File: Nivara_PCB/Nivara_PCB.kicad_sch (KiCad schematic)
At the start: 16 parts, among them J1 NPN_IN, J11 RELAY, J12 Analaog_In, J2 PNP_IN, J3 D_IN, J4 Analaog_In, J5 RUN/STOP, J6 FUENTE, J7 NPN_OUT, J8 PNP_OUT, J9 RS485, U4 2920L185DR

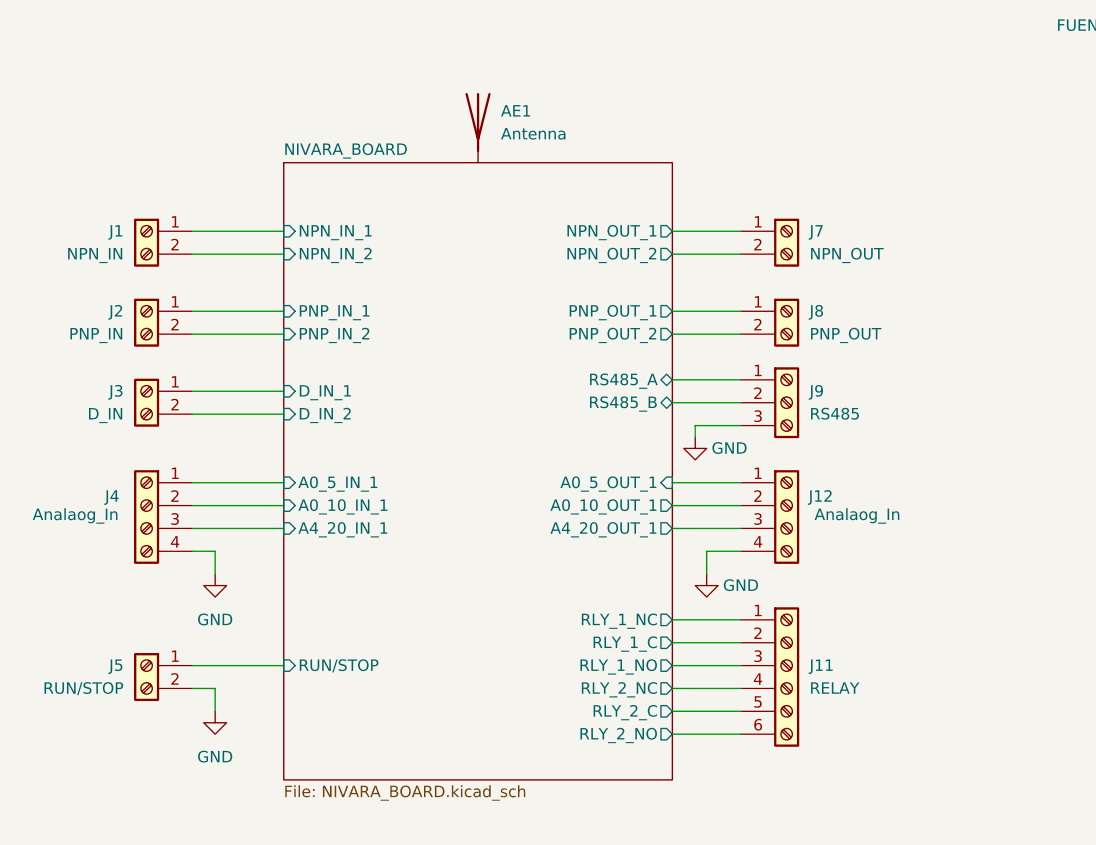
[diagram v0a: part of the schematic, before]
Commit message: Cambios en las mediciones análogas.
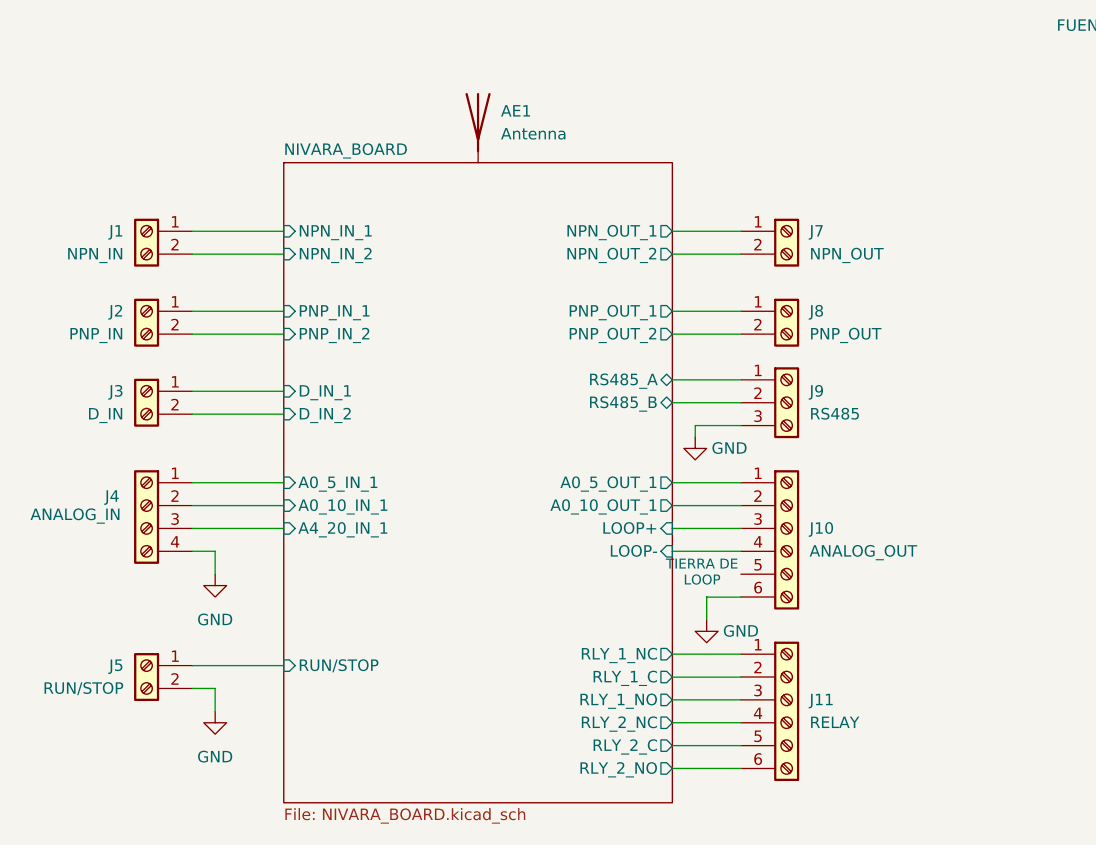
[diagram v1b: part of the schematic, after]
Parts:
- removed J12: Analaog_In, TerminalBlock:TerminalBlock_bornier-4_P5.08mm, symbol Connector:Screw_Terminal_01x04
- added J10: ANALOG_OUT, TerminalBlock:TerminalBlock_bornier-6_P5.08mm, symbol Connector:Screw_Terminal_01x06
- J4: value Analaog_In -> ANALOG_IN
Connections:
- net GND: now also J10.6 (Pin_6)
- net NIVARA_BOARD/A0_10_OUT_1: now also J10.2 (Pin_2)
- net NIVARA_BOARD/A0_5_OUT_1: now also J10.1 (Pin_1)
- new net NIVARA_BOARD/LOOP+: J10.3 (Pin_3)
- new net NIVARA_BOARD/LOOP-: J10.4 (Pin_4)
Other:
- sheet NIVARA_BOARD ports: added LOOP+, LOOP-; removed A4_20_OUT_1
- note added: "TIERRA DE LOOP"
- moved on the sheet: J11
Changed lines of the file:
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@@
+		)
+	)
+	(text "TIERRA DE\nLOOP"
+		(exclude_from_sim no)
+		(at 87.122 106.68 0)
+		(effects
+			(font
+				(size 1.1 1.1)
+			)
 		)
 	)
@@
 	(wire
 		(pts
+			(xy 87.63 109.22) (xy 91.44 109.22)
+		)
+		(stroke
+			(width 0)
+			(type default)
+		)
+	)
+	(wire
+		(pts
 			(xy 83.82 87.63) (xy 91.44 87.63)
 		)
@@
 	(wire
 		(pts
-			(xy 83.82 119.38) (xy 91.44 119.38)
+			(xy 83.82 123.19) (xy 91.44 123.19)
 		)
 		(stroke
@@
 	(wire
 		(pts
-			(xy 83.82 121.92) (xy 91.44 121.92)
+			(xy 83.82 125.73) (xy 91.44 125.73)
 		)
 		(stroke
@@
 	(wire
 		(pts
-			(xy 83.82 114.3) (xy 91.44 114.3)
+			(xy 83.82 118.11) (xy 91.44 118.11)
 		)
 		(stroke
@@
 	(wire
 		(pts
+			(xy 83.82 104.14) (xy 91.44 104.14)
+		)
+		(stroke
+			(width 0)
+			(type default)
+		)
+	)
+	(wire
+		(pts
 			(xy 83.82 101.6) (xy 91.44 101.6)
 		)
@@
 	(wire
 		(pts
-			(xy 83.82 116.84) (xy 91.44 116.84)
+			(xy 83.82 120.65) (xy 91.44 120.65)
 		)
 		(stroke
@@
 	(wire
 		(pts
-			(xy 83.82 111.76) (xy 91.44 111.76)
+			(xy 83.82 115.57) (xy 91.44 115.57)
 		)
 		(stroke
@@
 	(wire
 		(pts
-			(xy 87.63 104.14) (xy 91.44 104.14)
-		)
-		(stroke
-			(width 0)
-			(type default)
-		)
-	)
-	(wire
-		(pts
-			(xy 87.63 106.68) (xy 87.63 104.14)
-		)
-		(stroke
-			(width 0)
-			(type default)
-		)
-	)
-	(wire
-		(pts
-			(xy 83.82 124.46) (xy 91.44 124.46)
+			(xy 87.63 111.76) (xy 87.63 109.22)
+		)
+		(stroke
+			(width 0)
+			(type default)
+		)
+	)
+	(wire
+		(pts
+			(xy 83.82 128.27) (xy 91.44 128.27)
 		)
 		(stroke
@@
 	)
 	(symbol
+		(lib_id "Connector:Screw_Terminal_01x06")
+		(at 96.52 101.6 0)
+		(unit 1)
+		(exclude_from_sim no)
+		(in_bom yes)
+		(on_board yes)
+		(dnp no)
+		(property "Reference" "J10"
+			(at 99.06 101.5999 0)
+			(effects
+				(font
+					(size 1.27 1.27)
+				)
+				(justify left)
+			)
+		)
+		(property "Value" "ANALOG_OUT"
+			(at 99.06 104.1399 0)
+			(effects
+				(font
+					(size 1.27 1.27)
+				)
+				(justify left)
+			)
+		)
+		(property "Footprint" "TerminalBlock:TerminalBlock_bornier-6_P5.08mm"
+			(at 96.52 101.6 0)
+			(effects
+				(font
+					(size 1.27 1.27)
+				)
+				(hide yes)
+			)
+		)
+		(property "Datasheet" "~"
+			(at 96.52 101.6 0)
+			(effects
+				(font
+					(size 1.27 1.27)
+				)
+				(hide yes)
+			)
+		)
+		(property "Description" "Generic screw terminal, single row, 01x06, script generated (kicad-library-utils/schlib/autogen/connector/)"
+			(at 96.52 101.6 0)
+			(effects
+				(font
+					(size 1.27 1.27)
+				)
+				(hide yes)
+			)
+		)
+		(pin "4"
+		)
+		(pin "1"
+		)
+		(pin "6"
+		)
+		(pin "3"
+		)
+		(pin "5"
+		)
+		(pin "2"
+		)
+		(instances
+			(project "Nivara_PCB"
+				(path "/13184db0-a71d-4054-b13a-bbf46d2b100d"
+					(reference "J10")
+					(unit 1)
+				)
+			)
+		)
+	)
+	(symbol
 		(lib_id "power:GND")
 		(at 173.99 102.87 0)
@@
 	(symbol
 		(lib_id "power:GND")
-		(at 87.63 106.68 0)
+		(at 87.63 111.76 0)
 		(unit 1)
 		(exclude_from_sim no)
@@
 		(dnp no)
 		(property "Reference" "#PWR06"
-			(at 87.63 113.03 0)
+			(at 87.63 118.11 0)
 			(effects
 				(font
@@
 		)
 		(property "Value" "GND"
-			(at 91.44 107.95 0)
+			(at 91.44 113.03 0)
 			(effects
 				(font
@@
 		)
 		(property "Footprint" ""
-			(at 87.63 106.68 0)
+			(at 87.63 111.76 0)
 			(effects
 				(font
@@
 		)
 		(property "Datasheet" ""
-			(at 87.63 106.68 0)
+			(at 87.63 111.76 0)
 			(effects
 				(font
@@
 		)
 		(property "Description" "Power symbol creates a global label with name \"GND\" , ground"
-			(at 87.63 106.68 0)
+			(at 87.63 111.76 0)
 			(effects
 				(font
@@
 	(symbol
 		(lib_id "Connector:Screw_Terminal_01x06")
-		(at 96.52 116.84 0)
+		(at 96.52 120.65 0)
 		(unit 1)
 		(exclude_from_sim no)
@@
 		(dnp no)
 		(property "Reference" "J11"
-			(at 99.06 116.8399 0)
+			(at 99.06 120.6499 0)
 			(effects
 				(font
@@
 		)
 		(property "Value" "RELAY"
-			(at 99.06 119.3799 0)
+			(at 99.06 123.1899 0)
 			(effects
 				(font
@@
 		)
 		(property "Footprint" "TerminalBlock:TerminalBlock_bornier-6_P5.08mm"
-			(at 96.52 116.84 0)
+			(at 96.52 120.65 0)
 			(effects
 				(font
@@
 		)
 		(property "Datasheet" "~"
-			(at 96.52 116.84 0)
+			(at 96.52 120.65 0)
 			(effects
 				(font
@@
 		)
 		(property "Description" "Generic screw terminal, single row, 01x06, script generated (kicad-library-utils/schlib/autogen/connector/)"
-			(at 96.52 116.84 0)
+			(at 96.52 120.65 0)
 			(effects
 				(font
@@
 			)
 		)
-		(property "Value" "Analaog_In"
+		(property "Value" "ANALOG_IN"
 			(at 17.526 100.076 0)
 			(effects
@@
 				(path "/13184db0-a71d-4054-b13a-bbf46d2b100d"
 					(reference "J8")
-					(unit 1)
-				)
-			)
-		)
-	)
-	(symbol
-		(lib_id "Connector:Screw_Terminal_01x04")
-		(at 96.52 99.06 0)
-		(unit 1)
-		(exclude_from_sim no)
-		(in_bom yes)
-		(on_board yes)
-		(dnp no)
-		(property "Reference" "J12"
-			(at 100.33 98.044 0)
-			(effects
-				(font
-					(size 1.27 1.27)
-				)
-			)
-		)
-		(property "Value" "Analaog_In"
-			(at 104.394 100.076 0)
-			(effects
-				(font
-					(size 1.27 1.27)
-				)
-			)
-		)
-		(property "Footprint" "TerminalBlock:TerminalBlock_bornier-4_P5.08mm"
-			(at 96.52 99.06 0)
-			(effects
-				(font
-					(size 1.27 1.27)
-				)
-				(hide yes)
-			)
-		)
-		(property "Datasheet" "~"
-			(at 96.52 99.06 0)
-			(effects
-				(font
-					(size 1.27 1.27)
-				)
-				(hide yes)
-			)
-		)
-		(property "Description" "Generic screw terminal, single row, 01x04, script generated (kicad-library-utils/schlib/autogen/connector/)"
-			(at 96.52 99.06 0)
-			(effects
-				(font
-					(size 1.27 1.27)
-				)
-				(hide yes)
-			)
-		)
-		(pin "3"
-		)
-		(pin "2"
-		)
-		(pin "1"
-		)
-		(pin "4"
-		)
-		(instances
-			(project "Nivara_PCB"
-				(path "/13184db0-a71d-4054-b13a-bbf46d2b100d"
-					(reference "J12")
 					(unit 1)
 				)
@@
 	(sheet
 		(at 40.64 60.96)
-		(size 43.18 68.58)
+		(size 43.18 71.12)
 		(exclude_from_sim no)
 		(in_bom yes)
@@
 		)
 		(property "Sheetfile" "NIVARA_BOARD.kicad_sch"
-			(at 40.64 130.1246 0)
+			(at 40.64 132.6646 0)
 			(effects
 				(font
@@
 			)
 		)
-		(pin "A4_20_OUT_1" output
-			(at 83.82 101.6 0)
-			(effects
-				(font
-					(size 1.27 1.27)
-				)
-				(justify right)
-			)
-		)
 		(pin "D_IN_1" input
 			(at 40.64 86.36 180)
@@
 		)
 		(pin "RLY_1_C" output
-			(at 83.82 114.3 0)
+			(at 83.82 118.11 0)
 			(effects
 				(font
@@
 		)
 		(pin "RLY_1_NC" output
-			(at 83.82 111.76 0)
+			(at 83.82 115.57 0)
 			(effects
 				(font
@@
 		)
 		(pin "RLY_1_NO" output
-			(at 83.82 116.84 0)
+			(at 83.82 120.65 0)
 			(effects
 				(font
@@
 		)
 		(pin "RLY_2_C" output
-			(at 83.82 121.92 0)
+			(at 83.82 125.73 0)
 			(effects
 				(font
@@
 		)
 		(pin "RLY_2_NC" output
-			(at 83.82 119.38 0)
+			(at 83.82 123.19 0)
 			(effects
 				(font
@@
 		)
 		(pin "RLY_2_NO" output
-			(at 83.82 124.46 0)
+			(at 83.82 128.27 0)
 			(effects
 				(font
@@
 			)
 		)
-		(pin "A0_5_OUT_1" input
+		(pin "A0_5_OUT_1" output
 			(at 83.82 96.52 0)
 			(effects
 				(font
+					(size 1.27 1.27)
+				)
+				(justify right)
+			)
+		)
+		(pin "LOOP+" input
+			(at 83.82 101.6 0)
+			(effects
+				(font
+					(size 1.27 1.27)
+				)
+				(justify right)
+			)
+		)
+		(pin "LOOP-" input
+			(at 83.82 104.14 0)
+			(effects
+				(font

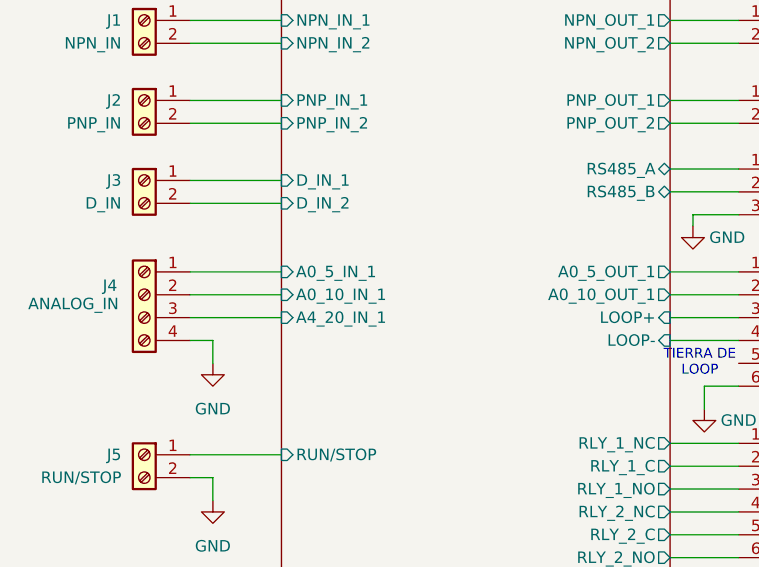
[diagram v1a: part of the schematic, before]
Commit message: Cambios en las salidas analogicas, ya que el ESP32 S3 no tiene DAC
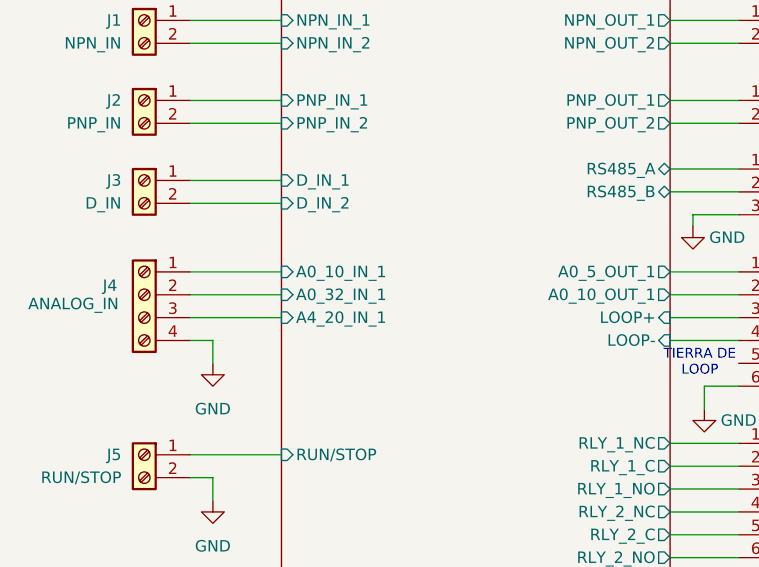
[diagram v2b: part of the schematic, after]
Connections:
- net NIVARA_BOARD/A0_5_IN_1 is gone; now on net NIVARA_BOARD/A0_10_IN_1: J4.1 (Pin_1)
- net NIVARA_BOARD/A0_10_IN_1: no longer J4.2 (Pin_2)
- new net NIVARA_BOARD/A0_32_IN_1: J4.2 (Pin_2)
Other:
- sheet NIVARA_BOARD ports: added A0_32_IN_1; removed A0_5_IN_1
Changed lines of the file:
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@@
+	(wire
+		(pts
+			(xy 33.02 121.92) (xy 33.02 119.38)
+		)
+		(stroke
+			(width 0)
+			(type default)
+		)
+	)
+	(wire
+		(pts
+			(xy 83.82 80.01) (xy 91.44 80.01)
+		)
+		(stroke
+			(width 0)
+			(type default)
+		)
+	)
+	(wire
+		(pts
+			(xy 160.02 43.18) (xy 160.02 52.07)
+		)
+		(stroke
+			(width 0)
+			(type default)
+		)
+	)
+	(wire
+		(pts
+			(xy 83.82 118.11) (xy 91.44 118.11)
+		)
+		(stroke
+			(width 0)
+			(type default)
+		)
+	)
+	(wire
+		(pts
+			(xy 83.82 96.52) (xy 91.44 96.52)
+		)
+		(stroke
+			(width 0)
+			(type default)
+		)
+	)
+	(wire
+		(pts
+			(xy 140.97 43.18) (xy 144.78 43.18)
+		)
+		(stroke
+			(width 0)
+			(type default)
+		)
+	)
+	(wire
+		(pts
+			(xy 83.82 104.14) (xy 91.44 104.14)
+		)
+		(stroke
+			(width 0)
+			(type default)
+		)
+	)
+	(wire
+		(pts
+			(xy 83.82 101.6) (xy 91.44 101.6)
+		)
+		(stroke
+			(width 0)
+			(type default)
+		)
+	)
+	(wire
+		(pts
+			(xy 160.02 35.56) (xy 160.02 43.18)
+		)
+		(stroke
+			(width 0)
+			(type default)
+		)
+	)
+	(wire
+		(pts
+			(xy 33.02 106.68) (xy 33.02 104.14)
+		)
+		(stroke
+			(width 0)
+			(type default)
+		)
+	)
+	(wire
+		(pts
+			(xy 83.82 99.06) (xy 91.44 99.06)
+		)
+		(stroke
+			(width 0)
+			(type default)
+		)
+	)
+	(wire
+		(pts
+			(xy 30.48 116.84) (xy 40.64 116.84)
+		)
+		(stroke
+			(width 0)
+			(type default)
+		)
+	)
+	(wire
+		(pts
+			(xy 30.48 96.52) (xy 40.64 96.52)
+		)
+		(stroke
+			(width 0)
+			(type default)
+		)
+	)
+	(wire
+		(pts
+			(xy 30.48 68.58) (xy 40.64 68.58)
+		)
+		(stroke
+			(width 0)
+			(type default)
+		)
+	)
+	(wire
+		(pts
+			(xy 86.36 91.44) (xy 86.36 90.17)
+		)
+		(stroke
+			(width 0)
+			(type default)
+		)
+	)
+	(wire
+		(pts
+			(xy 30.48 71.12) (xy 40.64 71.12)
+		)
+		(stroke
+			(width 0)
+			(type default)
+		)
+	)
+	(wire
+		(pts
+			(xy 162.56 90.17) (xy 162.56 93.98)
+		)
+		(stroke
+			(width 0)
+			(type default)
+		)
+	)
+	(wire
+		(pts
+			(xy 83.82 120.65) (xy 91.44 120.65)
+		)
+		(stroke
+			(width 0)
+			(type default)
+		)
+	)
+	(wire
+		(pts
+			(xy 83.82 71.12) (xy 91.44 71.12)
+		)
+		(stroke
+			(width 0)
+			(type default)
+		)
+	)
+	(wire
+		(pts
+			(xy 83.82 68.58) (xy 91.44 68.58)
+		)
+		(stroke
+			(width 0)
+			(type default)
+		)
+	)
+	(wire
+		(pts
+			(xy 83.82 85.09) (xy 91.44 85.09)
+		)
+		(stroke
+			(width 0)
+			(type default)
+		)
+	)
+	(wire
+		(pts
+			(xy 30.48 86.36) (xy 40.64 86.36)
+		)
+		(stroke
+			(width 0)
+			(type default)
+		)
+	)
+	(wire
+		(pts
+			(xy 30.48 80.01) (xy 40.64 80.01)
+		)
+		(stroke
+			(width 0)
+			(type default)
+		)
+	)
 	(wire
 		(pts
 			(xy 30.48 99.06) (xy 40.64 99.06)
-		)
-		(stroke
-			(width 0)
-			(type default)
-		)
-	)
-	(wire
-		(pts
-			(xy 33.02 121.92) (xy 33.02 119.38)
-		)
-		(stroke
-			(width 0)
-			(type default)
-		)
-	)
-	(wire
-		(pts
-			(xy 83.82 80.01) (xy 91.44 80.01)
-		)
-		(stroke
-			(width 0)
-			(type default)
-		)
-	)
-	(wire
-		(pts
-			(xy 160.02 43.18) (xy 160.02 52.07)
-		)
-		(stroke
-			(width 0)
-			(type default)
-		)
-	)
-	(wire
-		(pts
-			(xy 83.82 118.11) (xy 91.44 118.11)
-		)
-		(stroke
-			(width 0)
-			(type default)
-		)
-	)
-	(wire
-		(pts
-			(xy 83.82 96.52) (xy 91.44 96.52)
-		)
-		(stroke
-			(width 0)
-			(type default)
-		)
-	)
-	(wire
-		(pts
-			(xy 140.97 43.18) (xy 144.78 43.18)
-		)
-		(stroke
-			(width 0)
-			(type default)
-		)
-	)
-	(wire
-		(pts
-			(xy 83.82 104.14) (xy 91.44 104.14)
-		)
-		(stroke
-			(width 0)
-			(type default)
-		)
-	)
-	(wire
-		(pts
-			(xy 83.82 101.6) (xy 91.44 101.6)
-		)
-		(stroke
-			(width 0)
-			(type default)
-		)
-	)
-	(wire
-		(pts
-			(xy 160.02 35.56) (xy 160.02 43.18)
-		)
-		(stroke
-			(width 0)
-			(type default)
-		)
-	)
-	(wire
-		(pts
-			(xy 33.02 106.68) (xy 33.02 104.14)
-		)
-		(stroke
-			(width 0)
-			(type default)
-		)
-	)
-	(wire
-		(pts
-			(xy 30.48 96.52) (xy 40.64 96.52)
-		)
-		(stroke
-			(width 0)
-			(type default)
-		)
-	)
-	(wire
-		(pts
-			(xy 83.82 99.06) (xy 91.44 99.06)
-		)
-		(stroke
-			(width 0)
-			(type default)
-		)
-	)
-	(wire
-		(pts
-			(xy 30.48 116.84) (xy 40.64 116.84)
-		)
-		(stroke
-			(width 0)
-			(type default)
-		)
-	)
-	(wire
-		(pts
-			(xy 30.48 68.58) (xy 40.64 68.58)
-		)
-		(stroke
-			(width 0)
-			(type default)
-		)
-	)
-	(wire
-		(pts
-			(xy 86.36 91.44) (xy 86.36 90.17)
-		)
-		(stroke
-			(width 0)
-			(type default)
-		)
-	)
-	(wire
-		(pts
-			(xy 30.48 71.12) (xy 40.64 71.12)
-		)
-		(stroke
-			(width 0)
-			(type default)
-		)
-	)
-	(wire
-		(pts
-			(xy 162.56 90.17) (xy 162.56 93.98)
-		)
-		(stroke
-			(width 0)
-			(type default)
-		)
-	)
-	(wire
-		(pts
-			(xy 83.82 120.65) (xy 91.44 120.65)
-		)
-		(stroke
-			(width 0)
-			(type default)
-		)
-	)
-	(wire
-		(pts
-			(xy 83.82 71.12) (xy 91.44 71.12)
-		)
-		(stroke
-			(width 0)
-			(type default)
-		)
-	)
-	(wire
-		(pts
-			(xy 83.82 68.58) (xy 91.44 68.58)
-		)
-		(stroke
-			(width 0)
-			(type default)
-		)
-	)
-	(wire
-		(pts
-			(xy 83.82 85.09) (xy 91.44 85.09)
-		)
-		(stroke
-			(width 0)
-			(type default)
-		)
-	)
-	(wire
-		(pts
-			(xy 30.48 86.36) (xy 40.64 86.36)
-		)
-		(stroke
-			(width 0)
-			(type default)
-		)
-	)
-	(wire
-		(pts
-			(xy 30.48 80.01) (xy 40.64 80.01)
 		)
 		(stroke
@@
 		)
 		(pin "A0_10_IN_1" input
-			(at 40.64 99.06 180)
+			(at 40.64 96.52 180)
 			(effects
 				(font
@@
 			)
 		)
-		(pin "A0_5_IN_1" input
-			(at 40.64 96.52 180)
-			(effects
-				(font
+		(pin "A0_32_IN_1" input
+			(at 40.64 99.06 180)
+			(effects
+				(font
